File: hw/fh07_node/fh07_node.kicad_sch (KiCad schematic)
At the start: 0 parts

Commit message: Added ble lib outline
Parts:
- added U1: nRF54L15-QFXX, Package_DFN_QFN:QFN-48-1EP_6x6mm_P0.4mm_EP4.6x4.6mm, symbol PCM_nordic-lib-kicad-nrf54l:nRF54L15-QFXX
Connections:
- new net: U1.10 (VDD), U1.22 (VDD), U1.36 (VDD), U1.47 (VDD), U1.48 (VDD)
- new net: U1.32 (VSS_PA), U1.44 (VSS), U1.49 (VSS)
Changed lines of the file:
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@@
 	(generator_version "9.0")
 	(paper "A4")
+	(symbol
+		(lib_id "PCM_nordic-lib-kicad-nrf54l:nRF54L15-QFXX")
+		(at 115.57 95.25 0)
+		(unit 1)
+		(exclude_from_sim no)
+		(in_bom yes)
+		(on_board yes)
+		(dnp no)
+		(fields_autoplaced yes)
+		(property "Reference" "U1"
+			(at 115.57 95.25 0)
+			(do_not_autoplace yes)
+			(effects
+				(font
+					(size 1.27 1.27)
+				)
+			)
+		)
+		(property "Value" "nRF54L15-QFXX"
+			(at 115.57 97.79 0)
+			(do_not_autoplace yes)
+			(effects
+				(font
+					(size 1.27 1.27)
+				)
+			)
+		)
+		(property "Footprint" "Package_DFN_QFN:QFN-48-1EP_6x6mm_P0.4mm_EP4.6x4.6mm"
+			(at 115.57 168.91 0)
+			(effects
+				(font
+					(size 1.27 1.27)
+				)
+				(hide yes)
+			)
+		)
+		(property "Datasheet" "https://docs.nordicsemi.com/bundle/ps_nrf54L15"
+			(at 115.57 171.45 0)
+			(effects
+				(font
+					(size 1.27 1.27)
+				)
+				(hide yes)
+			)
+		)
+		(property "Description" "nRF54L Dual Core Multiprotocol BLE SoC"
+			(at 115.57 166.37 0)
+			(effects
+				(font
+					(size 1.27 1.27)
+				)
+				(hide yes)
+			)
+		)
+		(pin "46"
+		)
+		(pin "33"
+		)
+		(pin "44"
+		)
+		(pin "38"
+		)
+		(pin "40"
+		)
+		(pin "45"
+		)
+		(pin "32"
+		)
+		(pin "30"
+		)
+		(pin "1"
+		)
+		(pin "28"
+		)
+		(pin "23"
+		)
+		(pin "35"
+		)
+		(pin "24"
+		)
+		(pin "31"
+		)
+		(pin "25"
+		)
+		(pin "29"
+		)
+		(pin "2"
+		)
+		(pin "34"
+		)
+		(pin "4"
+		)
+		(pin "5"
+		)
+		(pin "6"
+		)
+		(pin "43"
+		)
+		(pin "8"
+		)
+		(pin "9"
+		)
+		(pin "27"
+		)
+		(pin "7"
+		)
+		(pin "37"
+		)
+		(pin "3"
+		)
+		(pin "39"
+		)
+		(pin "10"
+		)
+		(pin "14"
+		)
+		(pin "47"
+		)
+		(pin "41"
+		)
+		(pin "17"
+		)
+		(pin "11"
+		)
+		(pin "21"
+		)
+		(pin "20"
+		)
+		(pin "12"
+		)
+		(pin "36"
+		)
+		(pin "15"
+		)
+		(pin "19"
+		)
+		(pin "18"
+		)
+		(pin "13"
+		)
+		(pin "42"
+		)
+		(pin "16"
+		)
+		(pin "22"
+		)
+		(pin "48"
+		)
+		(pin "49"
+		)
+		(pin "26"
+		)
+		(instances
+			(project ""
+				(path "/aea54c0a-0593-4c80-97cc-583e63973e87"
+					(reference "U1")
+					(unit 1)
+				)
+			)
+		)
+	)
 	(sheet_instances
 		(path "/"

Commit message: Inited basic hardware schematic
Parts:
- removed U1: nRF54L15-QFXX, Package_DFN_QFN:QFN-48-1EP_6x6mm_P0.4mm_EP4.6x4.6mm, symbol PCM_nordic-lib-kicad-nrf54l:nRF54L15-QFXX
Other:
- added sheet MCU (nrf_mcu.kicad_sch)
- added sheet Power (power_converter.kicad_sch)
- added sheet Sensors (sensors.kicad_sch)
- title: (none) -> FH07 BLE Node
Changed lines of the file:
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@@
 	(generator_version "9.0")
 	(paper "A4")
-	(symbol
-		(lib_id "PCM_nordic-lib-kicad-nrf54l:nRF54L15-QFXX")
-		(at 115.57 95.25 0)
-		(unit 1)
+	(title_block
+		(title "FH07 BLE Node")
+		(date "2026-02-04")
+	)
+	(wire
+		(pts
+			(xy 104.14 110.49) (xy 104.14 123.19)
+		)
+		(stroke
+			(width 0)
+			(type default)
+		)
+	)
+	(wire
+		(pts
+			(xy 107.95 110.49) (xy 107.95 123.19)
+		)
+		(stroke
+			(width 0)
+			(type default)
+		)
+	)
+	(sheet
+		(at 161.29 60.96)
+		(size 66.04 49.53)
 		(exclude_from_sim no)
 		(in_bom yes)
@@
 		(dnp no)
 		(fields_autoplaced yes)
-		(property "Reference" "U1"
-			(at 115.57 95.25 0)
-			(do_not_autoplace yes)
+		(stroke
+			(width 0.1524)
+			(type solid)
+		)
+		(fill
+			(color 0 0 0 0.0000)
+		)
+		(property "Sheetname" "Power"
+			(at 161.29 60.2484 0)
 			(effects
 				(font
 					(size 1.27 1.27)
 				)
+				(justify left bottom)
 			)
 		)
-		(property "Value" "nRF54L15-QFXX"
-			(at 115.57 97.79 0)
-			(do_not_autoplace yes)
+		(property "Sheetfile" "power_converter.kicad_sch"
+			(at 161.29 111.0746 0)
 			(effects
 				(font
 					(size 1.27 1.27)
 				)
+				(justify left top)
 			)
 		)
-		(property "Footprint" "Package_DFN_QFN:QFN-48-1EP_6x6mm_P0.4mm_EP4.6x4.6mm"
-			(at 115.57 168.91 0)
+		(instances
+			(project "fh07_node"
+				(path "/aea54c0a-0593-4c80-97cc-583e63973e87"
+					(page "3")
+				)
+			)
+		)
+	)
+	(sheet
+		(at 62.23 60.96)
+		(size 82.55 49.53)
+		(exclude_from_sim no)
+		(in_bom yes)
+		(on_board yes)
+		(dnp no)
+		(fields_autoplaced yes)
+		(stroke
+			(width 0.1524)
+			(type solid)
+		)
+		(fill
+			(color 0 0 0 0.0000)
+		)
+		(property "Sheetname" "MCU"
+			(at 62.23 60.2484 0)
 			(effects
 				(font
 					(size 1.27 1.27)
 				)
-				(hide yes)
+				(justify left bottom)
 			)
 		)
-		(property "Datasheet" "https://docs.nordicsemi.com/bundle/ps_nrf54L15"
-			(at 115.57 171.45 0)
+		(property "Sheetfile" "nrf_mcu.kicad_sch"
+			(at 62.23 111.0746 0)
 			(effects
 				(font
 					(size 1.27 1.27)
 				)
-				(hide yes)
+				(justify left top)
 			)
 		)
-		(property "Description" "nRF54L Dual Core Multiprotocol BLE SoC"
-			(at 115.57 166.37 0)
+		(pin "SDA" input
+			(at 107.95 110.49 270)
 			(effects
 				(font
 					(size 1.27 1.27)
 				)
-				(hide yes)
+				(justify left)
 			)
 		)
-		(pin "46"
-		)
-		(pin "33"
-		)
-		(pin "44"
-		)
-		(pin "38"
-		)
-		(pin "40"
-		)
-		(pin "45"
-		)
-		(pin "32"
-		)
-		(pin "30"
-		)
-		(pin "1"
-		)
-		(pin "28"
-		)
-		(pin "23"
-		)
-		(pin "35"
-		)
-		(pin "24"
-		)
-		(pin "31"
-		)
-		(pin "25"
-		)
-		(pin "29"
-		)
-		(pin "2"
-		)
-		(pin "34"
-		)
-		(pin "4"
-		)
-		(pin "5"
-		)
-		(pin "6"
-		)
-		(pin "43"
-		)
-		(pin "8"
-		)
-		(pin "9"
-		)
-		(pin "27"
-		)
-		(pin "7"
-		)
-		(pin "37"
-		)
-		(pin "3"
-		)
-		(pin "39"
-		)
-		(pin "10"
-		)
-		(pin "14"
-		)
-		(pin "47"
-		)
-		(pin "41"
-		)
-		(pin "17"
-		)
-		(pin "11"
-		)
-		(pin "21"
-		)
-		(pin "20"
-		)
-		(pin "12"
-		)
-		(pin "36"
-		)
-		(pin "15"
-		)
-		(pin "19"
-		)
-		(pin "18"
-		)
-		(pin "13"
-		)
-		(pin "42"
-		)
-		(pin "16"
-		)
-		(pin "22"
-		)
-		(pin "48"
-		)
-		(pin "49"
-		)
-		(pin "26"
+		(pin "SCL" input
+			(at 104.14 110.49 270)
+			(effects
+				(font
+					(size 1.27 1.27)
+				)
+				(justify left)
+			)
 		)
 		(instances
-			(project ""
+			(project "fh07_node"
 				(path "/aea54c0a-0593-4c80-97cc-583e63973e87"
-					(reference "U1")
-					(unit 1)
+					(page "2")
 				)
 			)
+		)
+	)
+	(sheet
+		(at 62.23 123.19)
+		(size 81.28 39.37)
+		(exclude_from_sim no)
+		(in_bom yes)
+		(on_board yes)
+		(dnp no)
+		(fields_autoplaced yes)
+		(stroke
+			(width 0.1524)
+			(type solid)
+		)
+		(fill
+			(color 0 0 0 0.0000)
+		)
+		(property "Sheetname" "Sensors"
+			(at 62.23 122.4784 0)
+			(effects
+				(font
+					(size 1.27 1.27)
+				)
+				(justify left bottom)
+			)
+		)
+		(property "Sheetfile" "sensors.kicad_sch"
+			(at 62.23 163.1446 0)
+			(effects
+				(font
+					(size 1.27 1.27)
+				)
+				(justify left top)
+			)
+		)
+		(pin "SCL" input
+			(at 104.14 123.19 90)
+			(effects
+				(font
+					(size 1.27 1.27)
+				)
+				(justify right)
+			)
+		)
+		(pin "SDA" input
+			(at 107.95 123.19 90)
+			(effects
+				(font
+					(size 1.27 1.27)
+				)
+				(justify right)
+			)
+		)
+		(instances
+			(project "fh07_node"
+				(path "/aea54c0a-0593-4c80-97cc-583e63973e87"
+					(page "4")
+				)
+			)

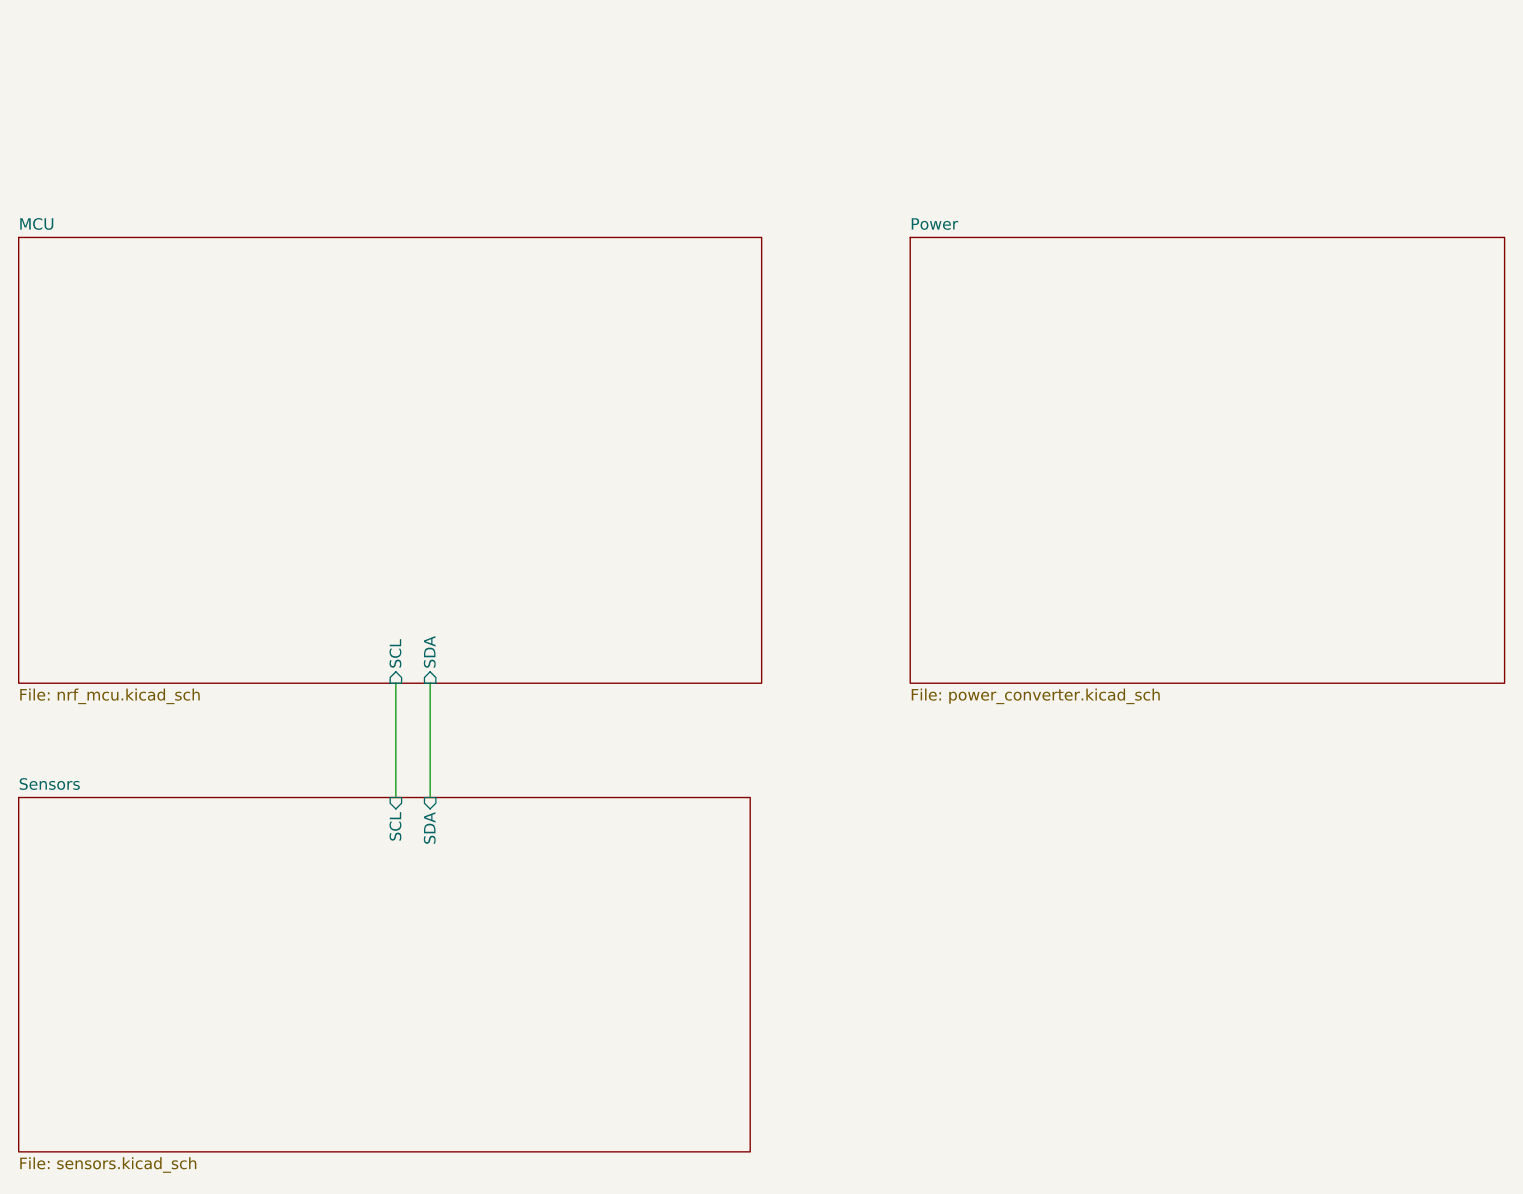
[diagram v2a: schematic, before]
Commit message: Updated sensor node and top level sheet
Fixed pin naming on sensor module and update MCU and Sensor top sheet
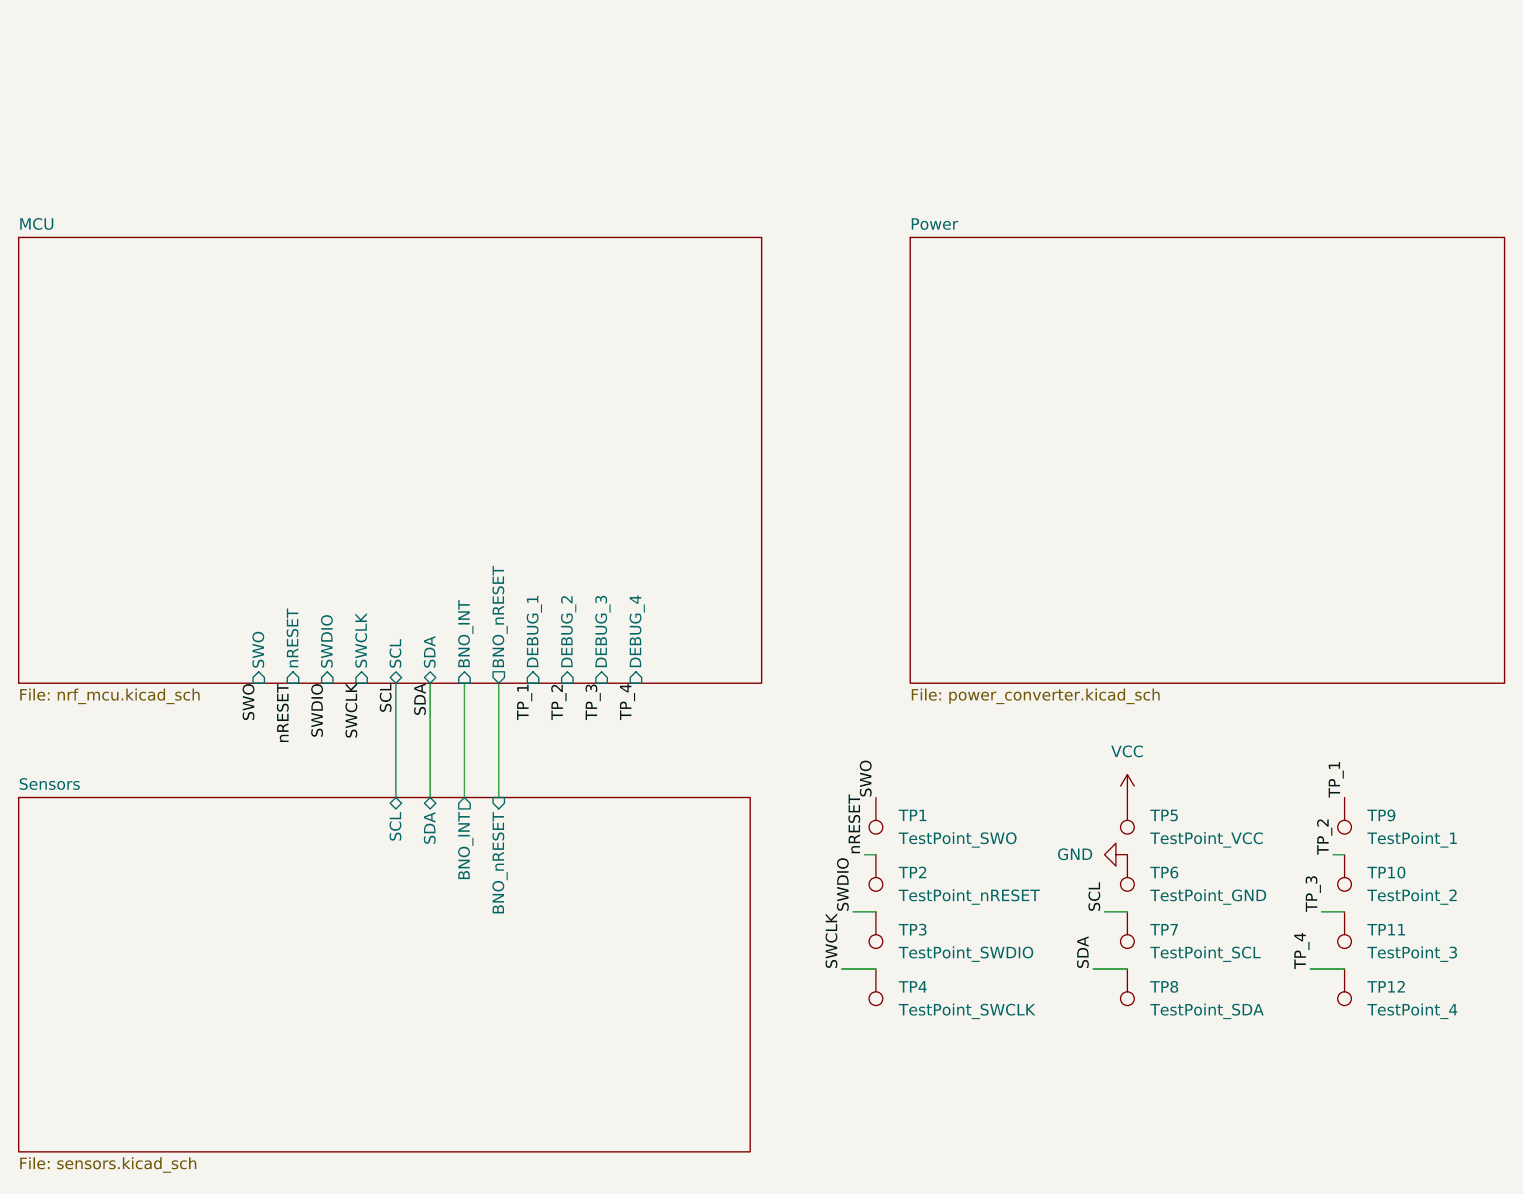
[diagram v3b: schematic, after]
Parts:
- added TP1: TestPoint_SWO, symbol Connector:TestPoint
- added TP10: TestPoint_2, symbol Connector:TestPoint
- added TP11: TestPoint_3, symbol Connector:TestPoint
- added TP12: TestPoint_4, symbol Connector:TestPoint
- added TP2: TestPoint_nRESET, symbol Connector:TestPoint
- added TP3: TestPoint_SWDIO, symbol Connector:TestPoint
- added TP4: TestPoint_SWCLK, symbol Connector:TestPoint
- added TP5: TestPoint_VCC, symbol Connector:TestPoint
- added TP6: TestPoint_GND, symbol Connector:TestPoint
- added TP7: TestPoint_SCL, symbol Connector:TestPoint
- added TP8: TestPoint_SDA, symbol Connector:TestPoint
- added TP9: TestPoint_1, symbol Connector:TestPoint
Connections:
- new net GND: TP6.1
- new net SCL: TP7.1
- new net SDA: TP8.1
- new net SWCLK: TP4.1
- new net SWDIO: TP3.1
- new net SWO: TP1.1
- new net TP_1: TP9.1
- new net TP_2: TP10.1
- new net TP_3: TP11.1
- new net TP_4: TP12.1
- new net VCC: TP5.1
- new net nRESET: TP2.1
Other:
- sheet MCU ports: added BNO_INT, BNO_nRESET, DEBUG_1, DEBUG_2, DEBUG_3, DEBUG_4, SWCLK, SWDIO, SWO, nRESET; removed none
- sheet Sensors ports: added BNO_INT, BNO_nRESET; removed none

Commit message: Completed hardware revision 1 release
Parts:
- TP1, TP10, TP11, TP12, TP2, TP3, TP4, TP5, TP6, TP7, TP8, TP9: footprint (none) -> TestPoint:TestPoint_THTPad_1.0x1.0mm_Drill0.5mm
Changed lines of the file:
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@@
 			)
 		)
-		(property "Footprint" ""
+		(property "Footprint" "TestPoint:TestPoint_THTPad_1.0x1.0mm_Drill0.5mm"
 			(at 152.4 123.19 0)
 			(effects
@@
 			)
 		)
-		(property "Footprint" ""
+		(property "Footprint" "TestPoint:TestPoint_THTPad_1.0x1.0mm_Drill0.5mm"
 			(at 204.47 123.19 0)
 			(effects
@@
 			)
 		)
-		(property "Footprint" ""
+		(property "Footprint" "TestPoint:TestPoint_THTPad_1.0x1.0mm_Drill0.5mm"
 			(at 180.34 123.19 0)
 			(effects
@@
 			)
 		)
-		(property "Footprint" ""
+		(property "Footprint" "TestPoint:TestPoint_THTPad_1.0x1.0mm_Drill0.5mm"
 			(at 152.4 129.54 0)
 			(effects
@@
 			)
 		)
-		(property "Footprint" ""
+		(property "Footprint" "TestPoint:TestPoint_THTPad_1.0x1.0mm_Drill0.5mm"
 			(at 180.34 142.24 0)
 			(effects
@@
 			)
 		)
-		(property "Footprint" ""
+		(property "Footprint" "TestPoint:TestPoint_THTPad_1.0x1.0mm_Drill0.5mm"
 			(at 204.47 129.54 0)
 			(effects
@@
 			)
 		)
-		(property "Footprint" ""
+		(property "Footprint" "TestPoint:TestPoint_THTPad_1.0x1.0mm_Drill0.5mm"
 			(at 204.47 142.24 0)
 			(effects
@@
 			)
 		)
-		(property "Footprint" ""
+		(property "Footprint" "TestPoint:TestPoint_THTPad_1.0x1.0mm_Drill0.5mm"
 			(at 204.47 135.89 0)
 			(effects
@@
 			)
 		)
-		(property "Footprint" ""
+		(property "Footprint" "TestPoint:TestPoint_THTPad_1.0x1.0mm_Drill0.5mm"
 			(at 152.4 135.89 0)
 			(effects
@@
 			)
 		)
-		(property "Footprint" ""
+		(property "Footprint" "TestPoint:TestPoint_THTPad_1.0x1.0mm_Drill0.5mm"
 			(at 152.4 142.24 0)
 			(effects
@@
 			)
 		)
-		(property "Footprint" ""
+		(property "Footprint" "TestPoint:TestPoint_THTPad_1.0x1.0mm_Drill0.5mm"
 			(at 180.34 129.54 0)
 			(effects
@@
 			)
 		)
-		(property "Footprint" ""
+		(property "Footprint" "TestPoint:TestPoint_THTPad_1.0x1.0mm_Drill0.5mm"
 			(at 180.34 135.89 0)
 			(effects
